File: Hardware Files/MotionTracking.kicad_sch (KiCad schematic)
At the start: 7 parts, among them U1 LSM6DSV16XTR, U4 STM32F411RET6

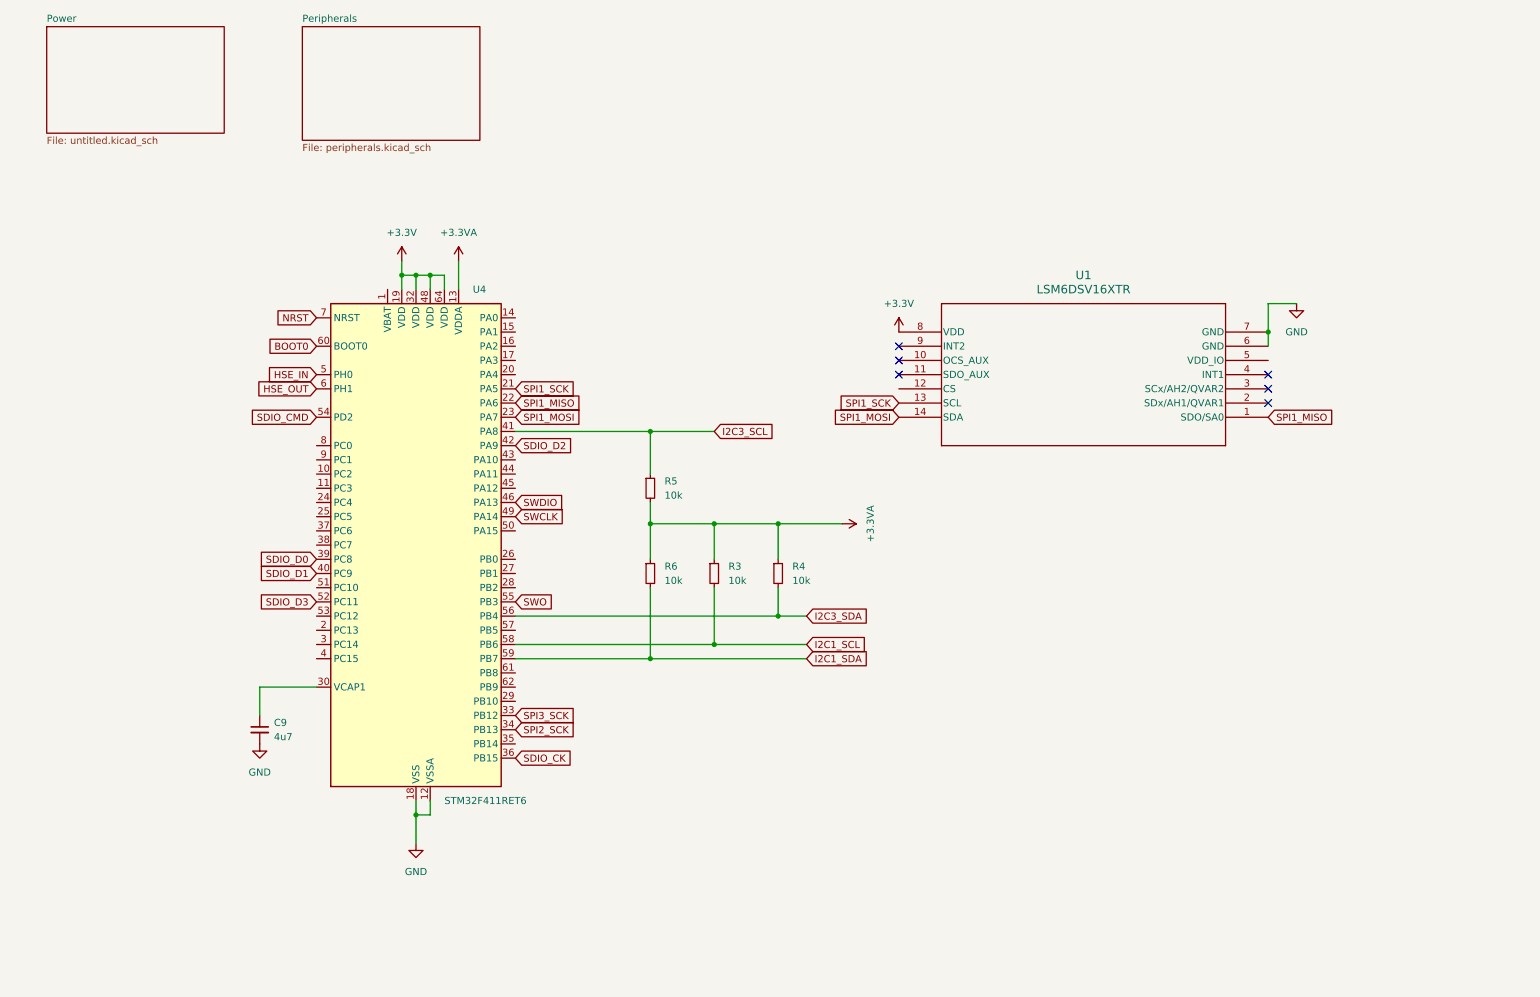
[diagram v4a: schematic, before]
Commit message: Adding CS for SPI and updated IOC file
- added CS on PA4
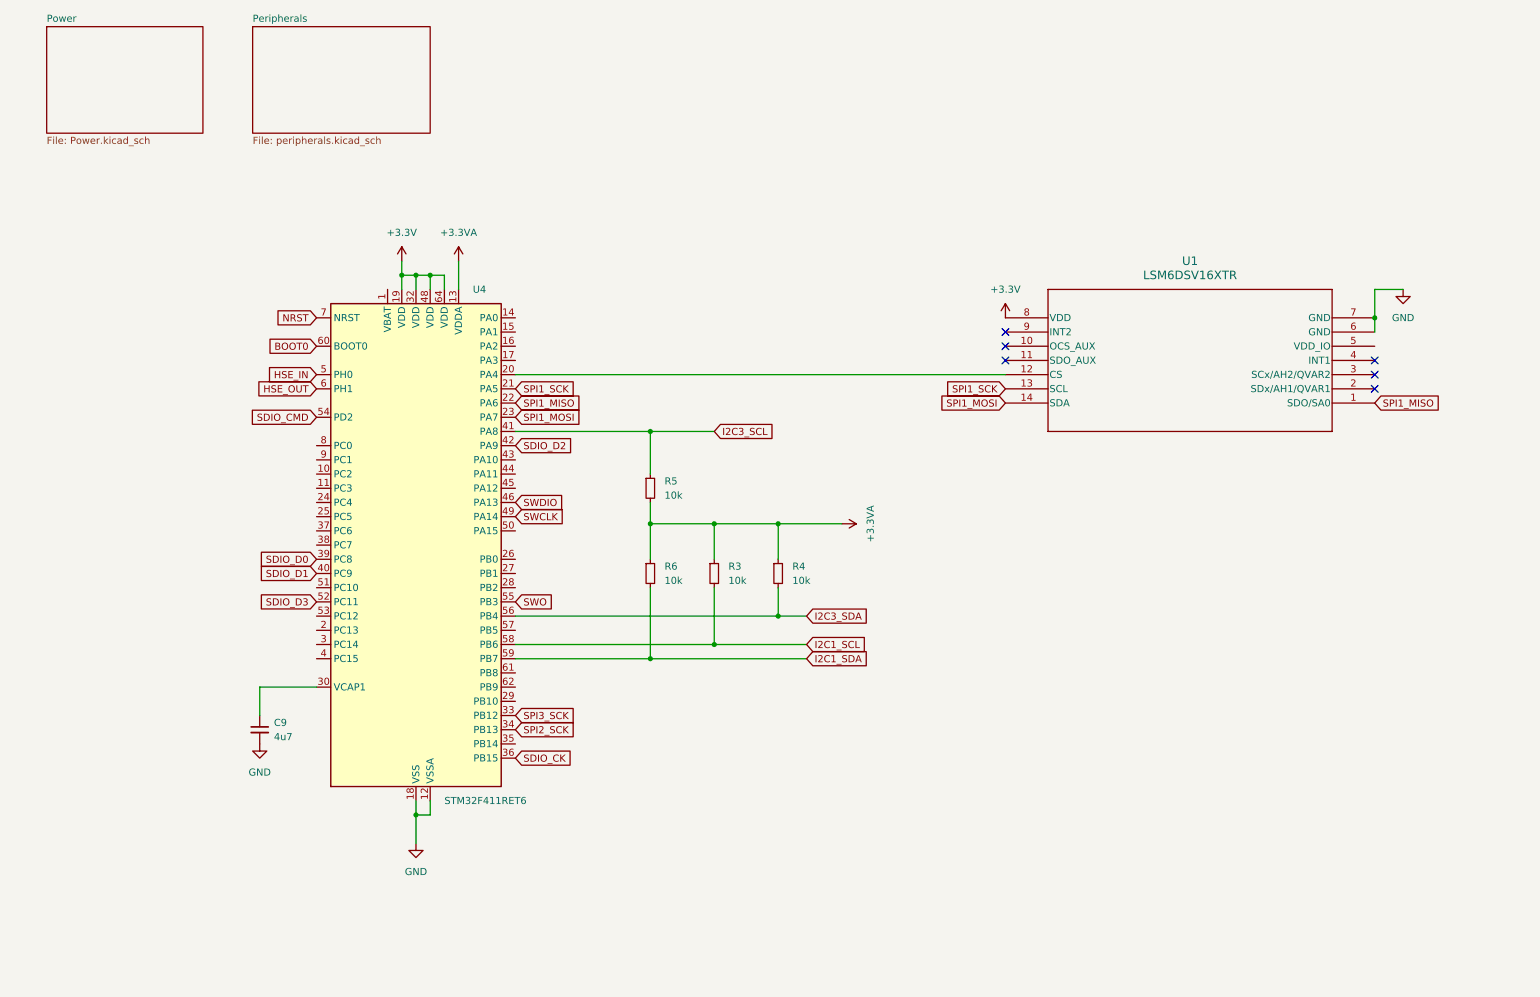
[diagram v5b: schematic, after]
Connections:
- net at U4.20 (PA4): now also U1.12 (CS)
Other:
- sheet Power: file untitled.kicad_sch -> Power.kicad_sch
- moved on the sheet: U1
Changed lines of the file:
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@@
   (junction (at 138.43 129.54) (diameter 0) (color 0 0 0 0)
   )
-  (junction (at 237.49 73.66) (diameter 0) (color 0 0 0 0)
+  (junction (at 256.54 71.12) (diameter 0) (color 0 0 0 0)
   )
   (junction (at 127 132.08) (diameter 0) (color 0 0 0 0)
@@
   (junction (at 138.43 107.95) (diameter 0) (color 0 0 0 0)
   )
-  (no_connect (at 237.49 83.82))
-  (no_connect (at 237.49 86.36))
-  (no_connect (at 171.45 78.74))
-  (no_connect (at 171.45 76.2))
-  (no_connect (at 171.45 81.28))
-  (no_connect (at 237.49 81.28))
+  (no_connect (at 256.54 81.28))
+  (no_connect (at 256.54 83.82))
+  (no_connect (at 190.5 76.2))
+  (no_connect (at 190.5 73.66))
+  (no_connect (at 190.5 78.74))
+  (no_connect (at 256.54 78.74))
   (wire (pts (xy 85.09 63.5) (xy 85.09 66.04))
     (stroke (width 0) (type default))
@@
     (stroke (width 0) (type default))
   )
+  (wire (pts (xy 102.87 81.28) (xy 190.5 81.28))
+    (stroke (width 0) (type default))
+  )
   (wire (pts (xy 90.17 63.5) (xy 90.17 66.04))
     (stroke (width 0) (type default))
@@
     (stroke (width 0) (type default))
   )
-  (wire (pts (xy 242.57 68.58) (xy 237.49 68.58))
-    (stroke (width 0) (type default))
-  )
-  (wire (pts (xy 237.49 68.58) (xy 237.49 73.66))
+  (wire (pts (xy 261.62 66.04) (xy 256.54 66.04))
+    (stroke (width 0) (type default))
+  )
+  (wire (pts (xy 256.54 66.04) (xy 256.54 71.12))
     (stroke (width 0) (type default))
   )
@@
     (stroke (width 0) (type default))
   )
-  (wire (pts (xy 237.49 73.66) (xy 237.49 76.2))
+  (wire (pts (xy 256.54 71.12) (xy 256.54 73.66))
     (stroke (width 0) (type default))
   )
@@
     )
   )
-  (global_label "SPI1_SCK" (shape input) (at 171.45 86.36 180) (fields_autoplaced)
-    (effects (font (size 1.27 1.27)) (justify right))
-    (property "Intersheetrefs" "${INTERSHEET_REFS}" (at 159.4539 86.36 0)
+  (global_label "SPI1_SCK" (shape input) (at 190.5 83.82 180) (fields_autoplaced)
+    (effects (font (size 1.27 1.27)) (justify right))
+    (property "Intersheetrefs" "${INTERSHEET_REFS}" (at 178.5039 83.82 0)
       (effects (font (size 1.27 1.27)) (justify right) hide)
     )
@@
     )
   )
-  (global_label "SPI1_MISO" (shape input) (at 237.49 88.9 0) (fields_autoplaced)
-    (effects (font (size 1.27 1.27)) (justify left))
-    (property "Intersheetrefs" "${INTERSHEET_REFS}" (at 250.3328 88.9 0)
+  (global_label "SPI1_MISO" (shape input) (at 256.54 86.36 0) (fields_autoplaced)
+    (effects (font (size 1.27 1.27)) (justify left))
+    (property "Intersheetrefs" "${INTERSHEET_REFS}" (at 269.3828 86.36 0)
       (effects (font (size 1.27 1.27)) (justify left) hide)
     )
@@
     )
   )
-  (global_label "SPI1_MOSI" (shape input) (at 171.45 88.9 180) (fields_autoplaced)
-    (effects (font (size 1.27 1.27)) (justify right))
-    (property "Intersheetrefs" "${INTERSHEET_REFS}" (at 158.6072 88.9 0)
+  (global_label "SPI1_MOSI" (shape input) (at 190.5 86.36 180) (fields_autoplaced)
+    (effects (font (size 1.27 1.27)) (justify right))
+    (property "Intersheetrefs" "${INTERSHEET_REFS}" (at 177.6572 86.36 0)
       (effects (font (size 1.27 1.27)) (justify right) hide)
     )
@@
     )
   )
-  (symbol (lib_id "power:GND") (at 242.57 68.58 0) (unit 1)
-    (in_bom yes) (on_board yes) (dnp no) (fields_autoplaced)
-    (property "Reference" "#PWR013" (at 242.57 74.93 0)
-      (effects (font (size 1.27 1.27)) hide)
-    )
-    (property "Value" "GND" (at 242.57 73.66 0)
+  (symbol (lib_id "power:GND") (at 261.62 66.04 0) (unit 1)
+    (in_bom yes) (on_board yes) (dnp no) (fields_autoplaced)
+    (property "Reference" "#PWR013" (at 261.62 72.39 0)
+      (effects (font (size 1.27 1.27)) hide)
+    )
+    (property "Value" "GND" (at 261.62 71.12 0)
       (effects (font (size 1.27 1.27)))
     )
-    (property "Footprint" "" (at 242.57 68.58 0)
-      (effects (font (size 1.27 1.27)) hide)
-    )
-    (property "Datasheet" "" (at 242.57 68.58 0)
+    (property "Footprint" "" (at 261.62 66.04 0)
+      (effects (font (size 1.27 1.27)) hide)
+    )
+    (property "Datasheet" "" (at 261.62 66.04 0)
       (effects (font (size 1.27 1.27)) hide)
     )
@@
     )
   )
-  (symbol (lib_id "imu:LSM6DSV16XTR") (at 237.49 88.9 180) (unit 1)
-    (in_bom yes) (on_board yes) (dnp no) (fields_autoplaced)
-    (property "Reference" "U1" (at 204.47 63.5 0)
+  (symbol (lib_id "imu:LSM6DSV16XTR") (at 256.54 86.36 180) (unit 1)
+    (in_bom yes) (on_board yes) (dnp no) (fields_autoplaced)
+    (property "Reference" "U1" (at 223.52 60.96 0)
       (effects (font (size 1.524 1.524)))
     )
-    (property "Value" "LSM6DSV16XTR" (at 204.47 66.04 0)
+    (property "Value" "LSM6DSV16XTR" (at 223.52 63.5 0)
       (effects (font (size 1.524 1.524)))
     )
-    (property "Footprint" "LGA14L_LSM6_STM" (at 237.49 88.9 0)
+    (property "Footprint" "LGA14L_LSM6_STM" (at 256.54 86.36 0)
       (effects (font (size 1.27 1.27) italic) hide)
     )
-    (property "Datasheet" "LSM6DSV16XTR" (at 237.49 88.9 0)
+    (property "Datasheet" "LSM6DSV16XTR" (at 256.54 86.36 0)
       (effects (font (size 1.27 1.27) italic) hide)
     )
@@
     )
   )
-  (symbol (lib_id "power:+3.3V") (at 171.45 73.66 0) (unit 1)
-    (in_bom yes) (on_board yes) (dnp no) (fields_autoplaced)
-    (property "Reference" "#PWR014" (at 171.45 77.47 0)
-      (effects (font (size 1.27 1.27)) hide)
-    )
-    (property "Value" "+3.3V" (at 171.45 68.58 0)
+  (symbol (lib_id "power:+3.3V") (at 190.5 71.12 0) (unit 1)
+    (in_bom yes) (on_board yes) (dnp no) (fields_autoplaced)
+    (property "Reference" "#PWR014" (at 190.5 74.93 0)
+      (effects (font (size 1.27 1.27)) hide)
+    )
+    (property "Value" "+3.3V" (at 190.5 66.04 0)
       (effects (font (size 1.27 1.27)))
     )
-    (property "Footprint" "" (at 171.45 73.66 0)
-      (effects (font (size 1.27 1.27)) hide)
-    )
-    (property "Datasheet" "" (at 171.45 73.66 0)
+    (property "Footprint" "" (at 190.5 71.12 0)
+      (effects (font (size 1.27 1.27)) hide)
+    )
+    (property "Datasheet" "" (at 190.5 71.12 0)
       (effects (font (size 1.27 1.27)) hide)
     )
@@
     )
   )
-  (sheet (at 19.05 19.05) (size 31.75 19.05) (fields_autoplaced)
+  (sheet (at 19.05 19.05) (size 27.94 19.05) (fields_autoplaced)
     (stroke (width 0.1524) (type solid))
     (fill (color 0 0 0 0.0000))
@@
       (effects (font (size 1.27 1.27)) (justify left bottom))
     )
-    (property "Sheetfile" "untitled.kicad_sch" (at 19.05 38.6846 0)
+    (property "Sheetfile" "Power.kicad_sch" (at 19.05 38.6846 0)
       (effects (font (size 1.27 1.27)) (justify left top))
     )
@@
     )
   )
-  (sheet (at 64.77 19.05) (size 31.75 20.32) (fields_autoplaced)
+  (sheet (at 55.88 19.05) (size 31.75 19.05) (fields_autoplaced)
     (stroke (width 0.1524) (type solid))
     (fill (color 0 0 0 0.0000))
-    (property "Sheetname" "Peripherals" (at 64.77 18.3384 0)
+    (property "Sheetname" "Peripherals" (at 55.88 18.3384 0)
       (effects (font (size 1.27 1.27)) (justify left bottom))
     )
-    (property "Sheetfile" "peripherals.kicad_sch" (at 64.77 39.9546 0)
+    (property "Sheetfile" "peripherals.kicad_sch" (at 55.88 38.6846 0)
       (effects (font (size 1.27 1.27)) (justify left top))
     )

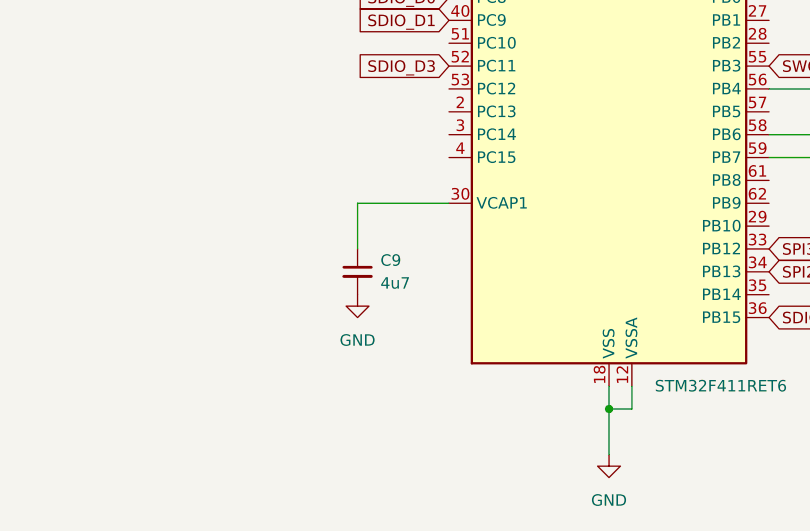
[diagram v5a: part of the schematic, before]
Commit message: STARTED PCB DESIGN!!
Footprints added to schematic components(some may need to be changed). Organized components and started some rough draft routing. Will most likely need some reorganization, how will parts affect each other(caps, inductors)? NEED TO ADD SOLDER POINTS for battery holder AND FOR 2 other IMUs.
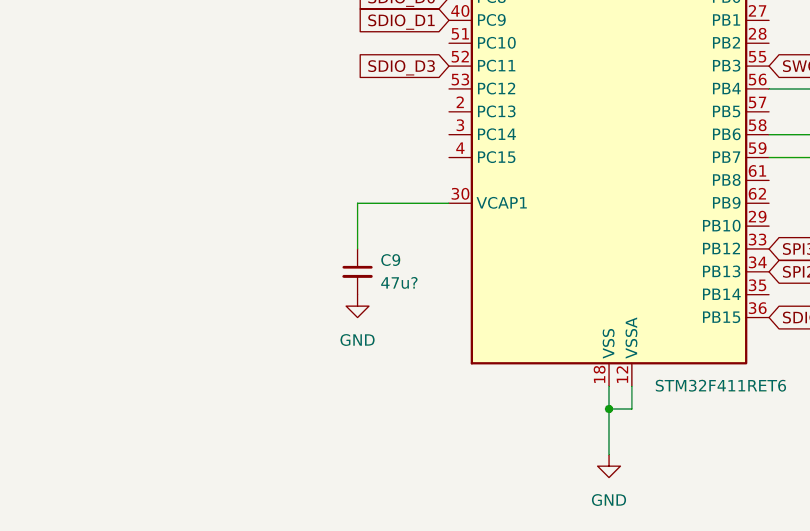
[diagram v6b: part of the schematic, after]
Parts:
- C9: value 4u7 -> 47u?; footprint (none) -> Capacitor_SMD:C_Elec_3x5.4
- R3, R4, R5, R6: footprint (none) -> Resistor_SMD:R_0201_0603Metric
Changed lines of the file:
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@@
       (effects (font (size 1.27 1.27)) (justify left))
     )
-    (property "Footprint" "" (at 127 101.6 0)
+    (property "Footprint" "Resistor_SMD:R_0201_0603Metric" (at 127 101.6 0)
       (effects (font (size 1.27 1.27)) hide)
     )
@@
       (effects (font (size 1.27 1.27)) (justify left))
     )
-    (property "Value" "4u7" (at 59.69 146.0563 0)
-      (effects (font (size 1.27 1.27)) (justify left))
-    )
-    (property "Footprint" "" (at 57.15 144.78 0)
+    (property "Value" "47u?" (at 59.69 146.0563 0)
+      (effects (font (size 1.27 1.27)) (justify left))
+    )
+    (property "Footprint" "Capacitor_SMD:C_Elec_3x5.4" (at 57.15 144.78 0)
       (effects (font (size 1.27 1.27)) hide)
     )
@@
       (effects (font (size 1.27 1.27)) (justify left))
     )
-    (property "Footprint" "" (at 149.86 116.84 0)
+    (property "Footprint" "Resistor_SMD:R_0201_0603Metric" (at 149.86 116.84 0)
       (effects (font (size 1.27 1.27)) hide)
     )
@@
       (effects (font (size 1.27 1.27)) (justify left))
     )
-    (property "Footprint" "" (at 127 116.84 0)
+    (property "Footprint" "Resistor_SMD:R_0201_0603Metric" (at 127 116.84 0)
       (effects (font (size 1.27 1.27)) hide)
     )
@@
       (effects (font (size 1.27 1.27)) (justify left))
     )
-    (property "Footprint" "" (at 138.43 116.84 0)
-      (effects (font (size 1.27 1.27)) hide)
-    )
+    (property "Footprint" "Resistor_SMD:R_0201_0603Metric" (at 138.43 116.84 0)
+      (effects (font (size 1.27 1.27)) hide)
+    )

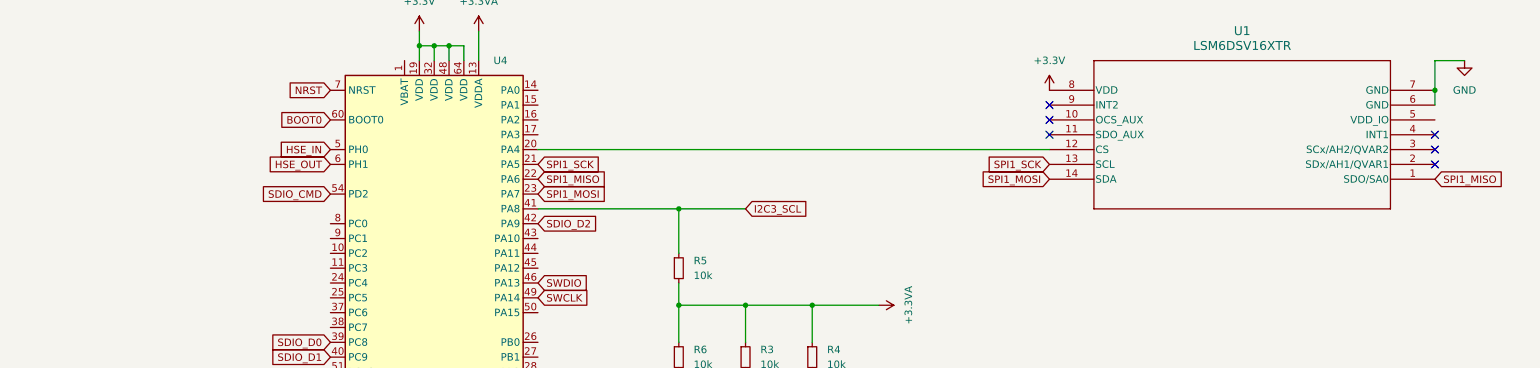
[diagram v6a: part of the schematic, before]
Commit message: Added comments
Added NC flag to the detect pin on SD reader. Left a comment to add NC flags into the MCU for all unused pins.
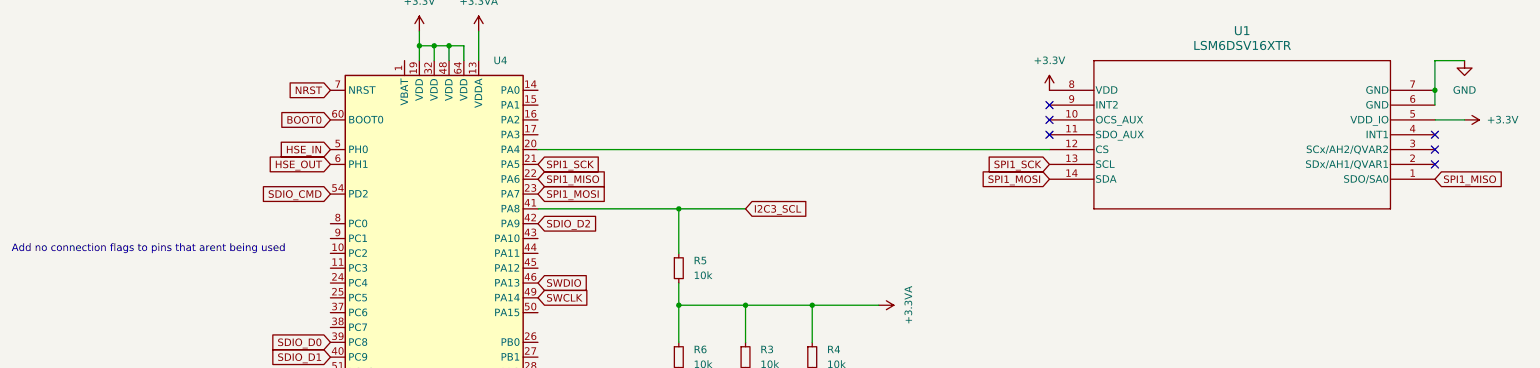
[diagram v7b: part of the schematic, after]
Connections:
- net +3.3V: now also U1.5 (VDD_IO)
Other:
- note added: "Add no connection flags to pins that arent being used"
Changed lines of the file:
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@@
+    (stroke (width 0) (type default))
+  )
+  (wire (pts (xy 256.54 76.2) (xy 261.62 76.2))
     (stroke (width 0) (type default))
   )
@@
   (wire (pts (xy 149.86 107.95) (xy 161.29 107.95))
     (stroke (width 0) (type default))
+  )
+  (text "Add no connection flags to pins that arent being used"
+    (at 12.7 99.06 0)
+    (effects (font (size 1.27 1.27)) (justify left bottom))
   )
   (global_label "SDIO_D2" (shape input) (at 102.87 93.98 0) (fields_autoplaced)
@@
         )
       )
+    )
+  )
+  (symbol (lib_id "power:+3.3V") (at 261.62 76.2 270) (unit 1)
+    (in_bom yes) (on_board yes) (dnp no) (fields_autoplaced)
+    (property "Reference" "#PWR023" (at 257.81 76.2 0)
+      (effects (font (size 1.27 1.27)) hide)
+    )
+    (property "Value" "+3.3V" (at 265.43 76.2 90)
+      (effects (font (size 1.27 1.27)) (justify left))
+    )
+    (property "Footprint" "" (at 261.62 76.2 0)
+      (effects (font (size 1.27 1.27)) hide)
+    )
+    (property "Datasheet" "" (at 261.62 76.2 0)
+      (effects (font (size 1.27 1.27)) hide)
+    )
+    (pin "1")
+    (instances
+      (project "MotionTracking"
+        (path "/111120b9-36de-4e64-8ed5-7419f276010e"
+          (reference "#PWR023") (unit 1)
+        )
+      )
